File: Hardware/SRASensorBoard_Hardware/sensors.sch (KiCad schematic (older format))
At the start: 10 parts

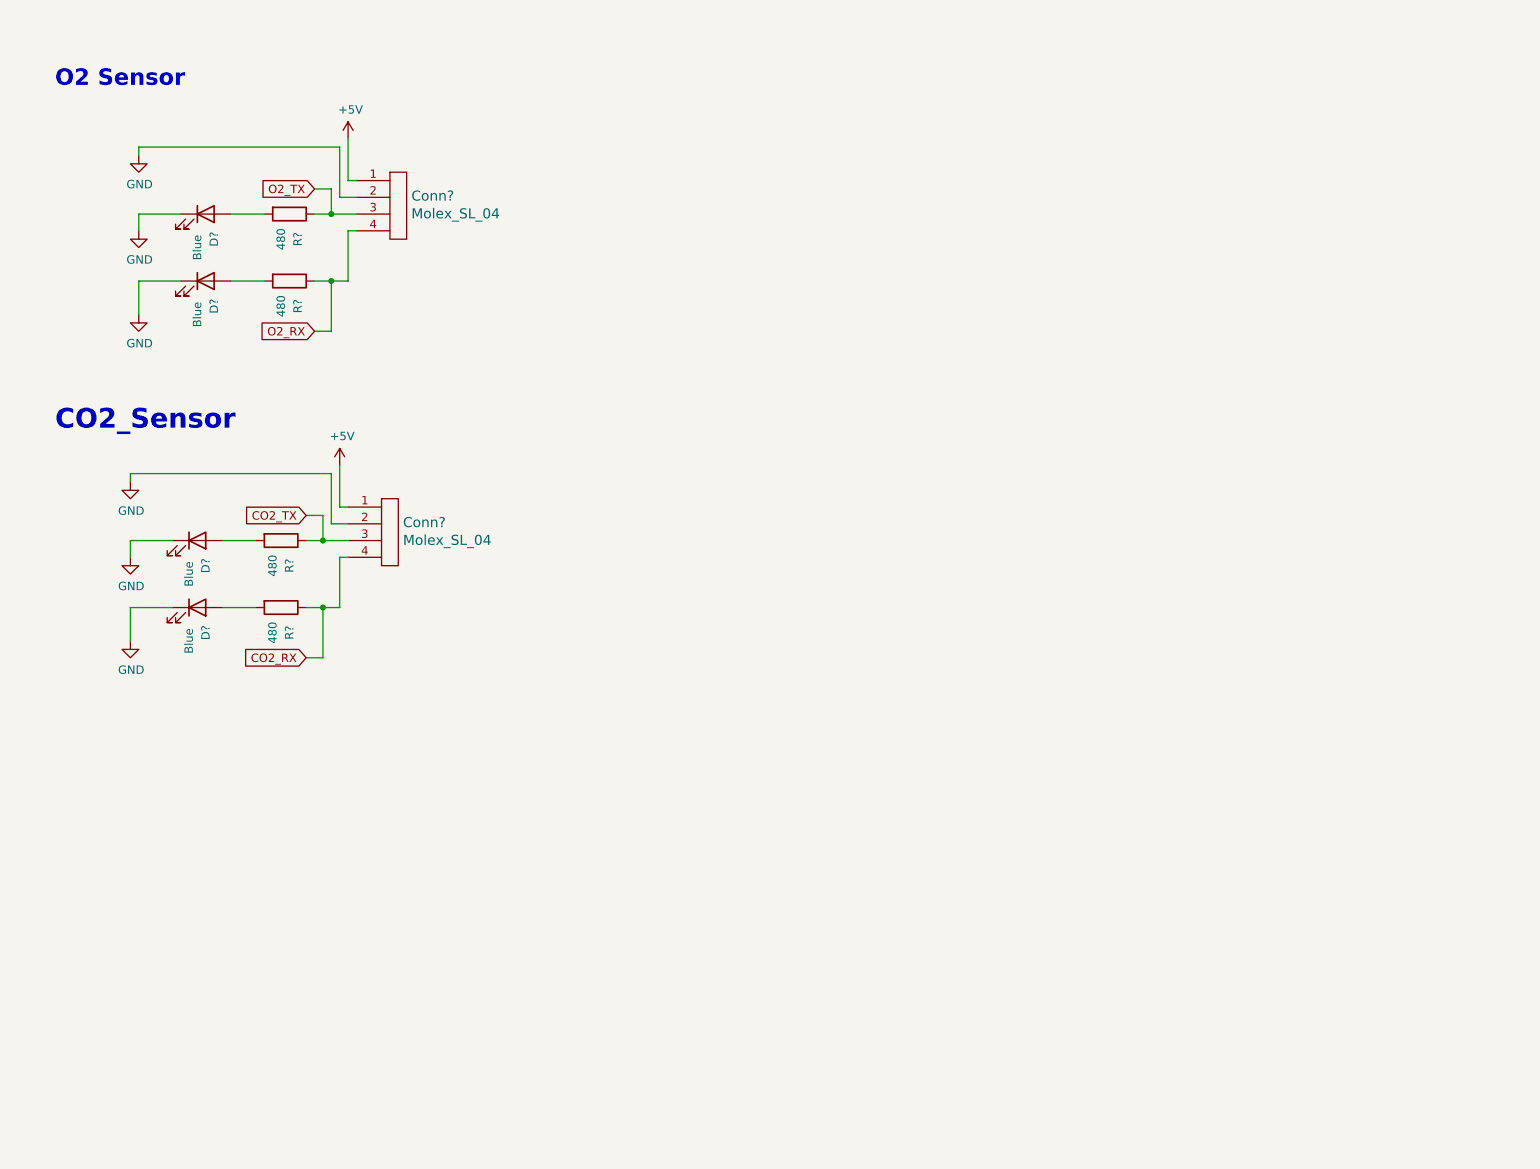
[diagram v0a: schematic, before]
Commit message: Methane Sensor & Tiva Pins added
Added USB A connector and USB to UART converter for CH4 sensor
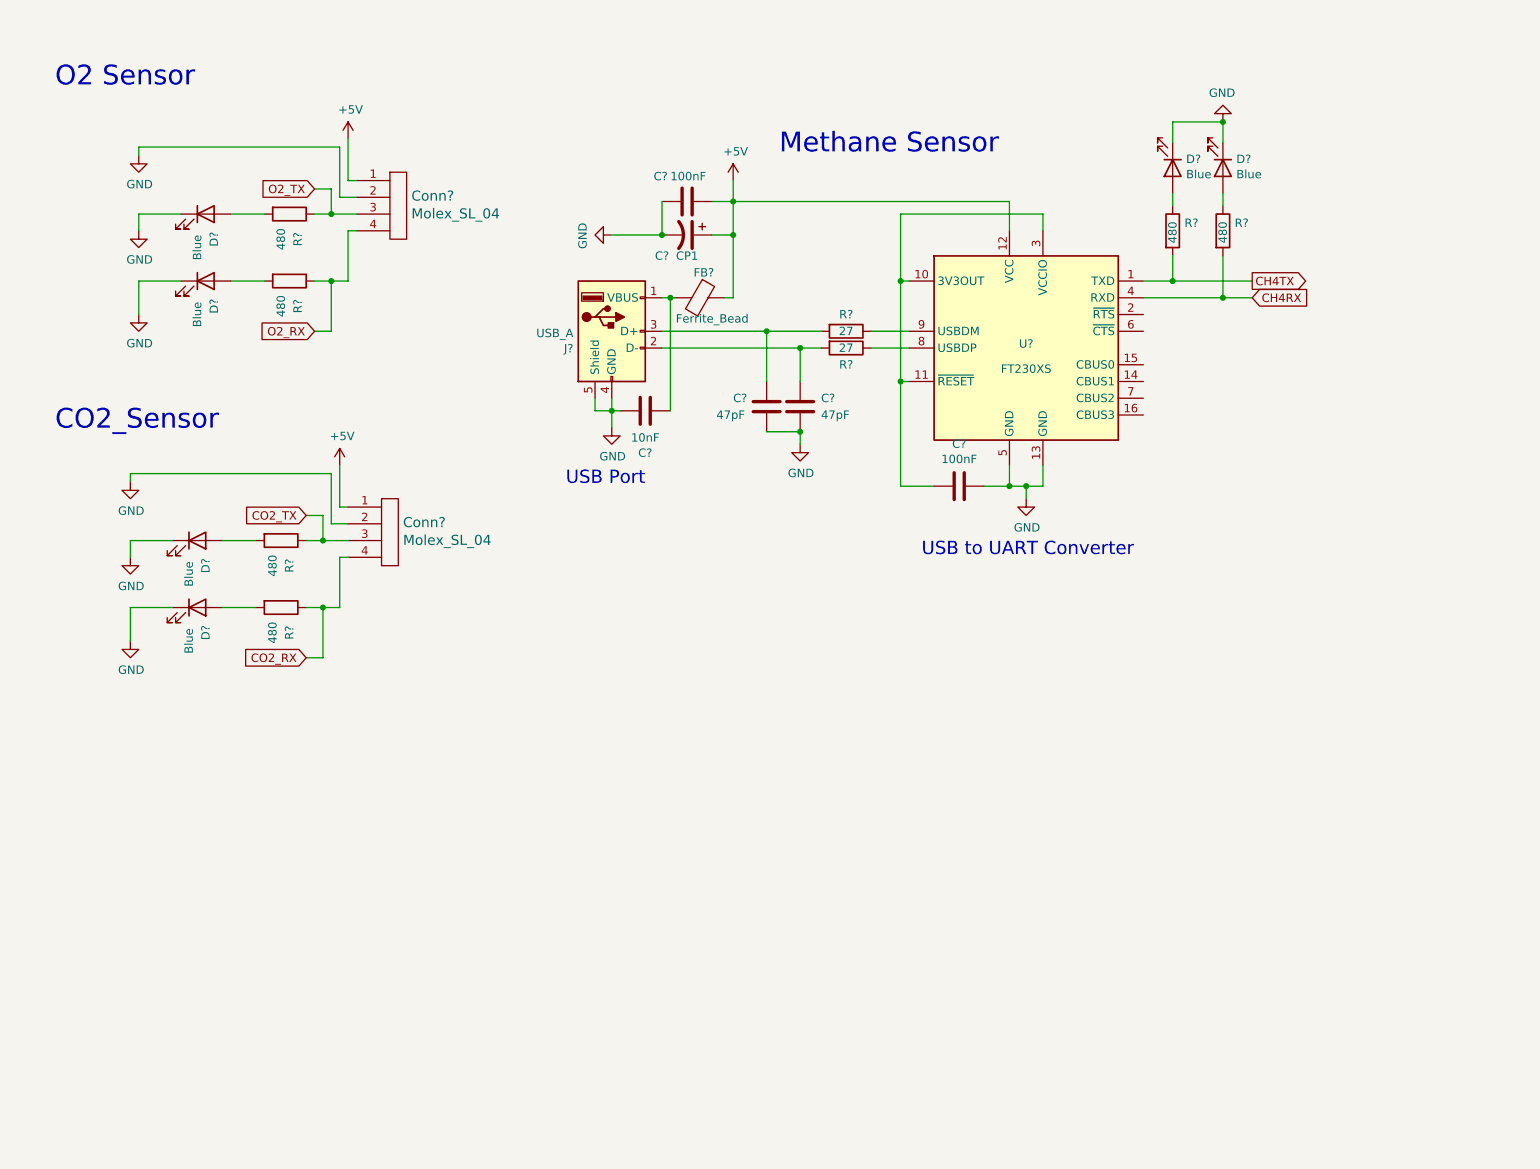
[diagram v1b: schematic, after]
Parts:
- added C?: 10nF, symbol Device:C
- added C? (x2): 47pF, symbol Device:C
- added C? (x2): 100nF, symbol Device:C
- added C?: CP1, symbol Device:CP1
- added D? (x2): Blue, symbol Device:LED
- added FB?: Ferrite_Bead, symbol Device:Ferrite_Bead
- added J?: USB_A, symbol Connector:USB_A
- added R? (x2): 27, symbol Device:R
- added R? (x2): 480, symbol Device:R
- added U?: FT230XS, Package_SO:SSOP-16_3.9x4.9mm_P0.635mm, symbol Interface_USB:FT230XS
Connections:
- net +5V: now also C?.1, C?.1, FB?.1, U?.12 (VCC)
- net GND: now also C?.1, C?.2, C?.2, C?.2, C?.2, C?.2, D?.1 (K), D?.1 (K), J?.4 (GND), J?.5 (Shield), U?.13 (GND), U?.5 (GND)
- new net: C?.1, U?.10 (3V3OUT), U?.11 (~RESET), U?.3 (VCCIO)
- new net: R?.1, U?.8 (USBDP)
- new net: R?.1, U?.9 (USBDM)
- new net: C?.2, FB?.2, J?.1 (VBUS)
- new net: C?.1, J?.2 (D-), R?.2
- new net: C?.1, J?.3 (D+), R?.2
- new net: D?.2 (A), R?.1 (x2)
- new net CH4RX: R?.2, U?.4 (RXD)
- new net CH4TX: R?.2, U?.1 (TXD)
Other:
- note added: "Methane Sensor"
- note added: "USB Port"
- note added: "USB to UART Converter"

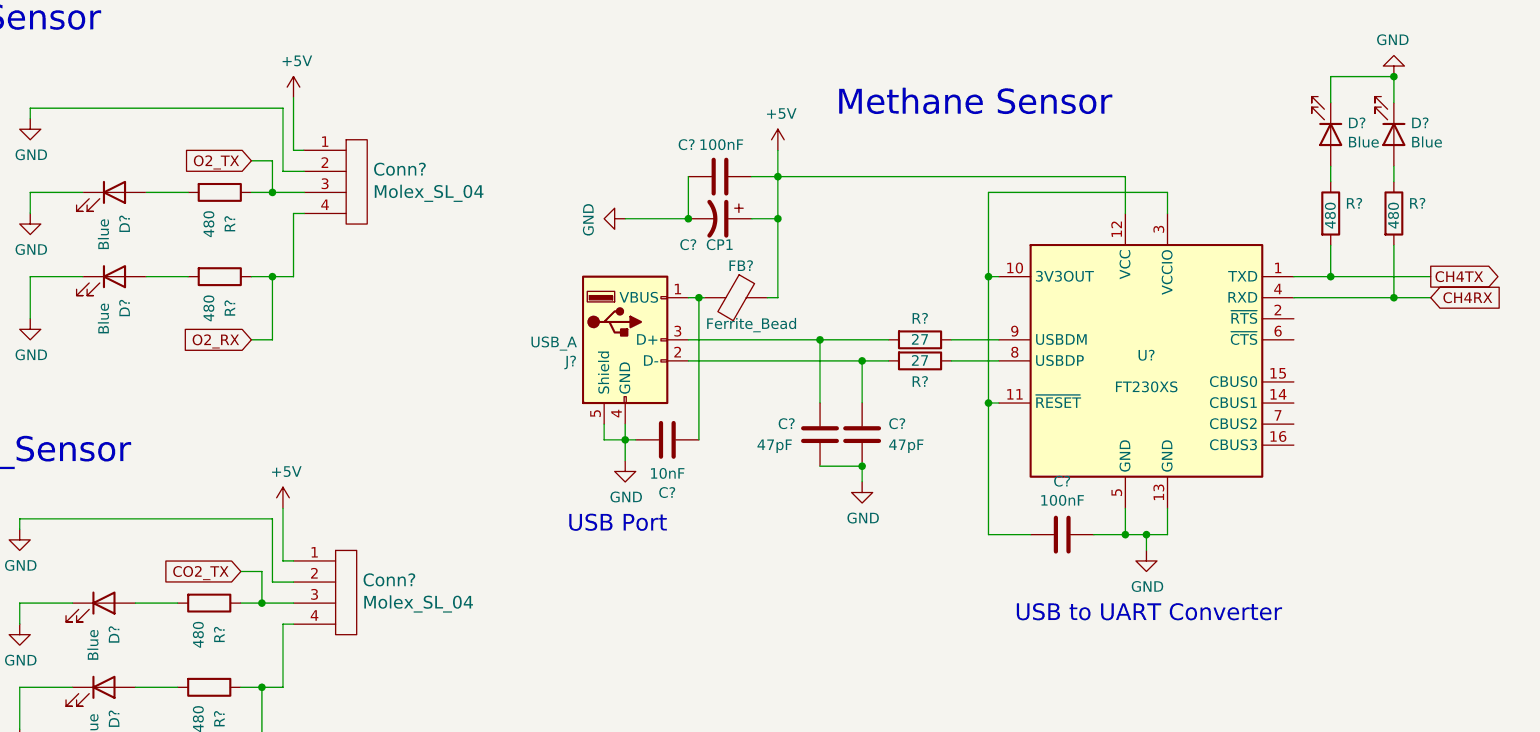
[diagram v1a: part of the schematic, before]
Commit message: Renamed CH4 RX/TX to match with others, swapped tx&rx tiva pins (might be wrong)
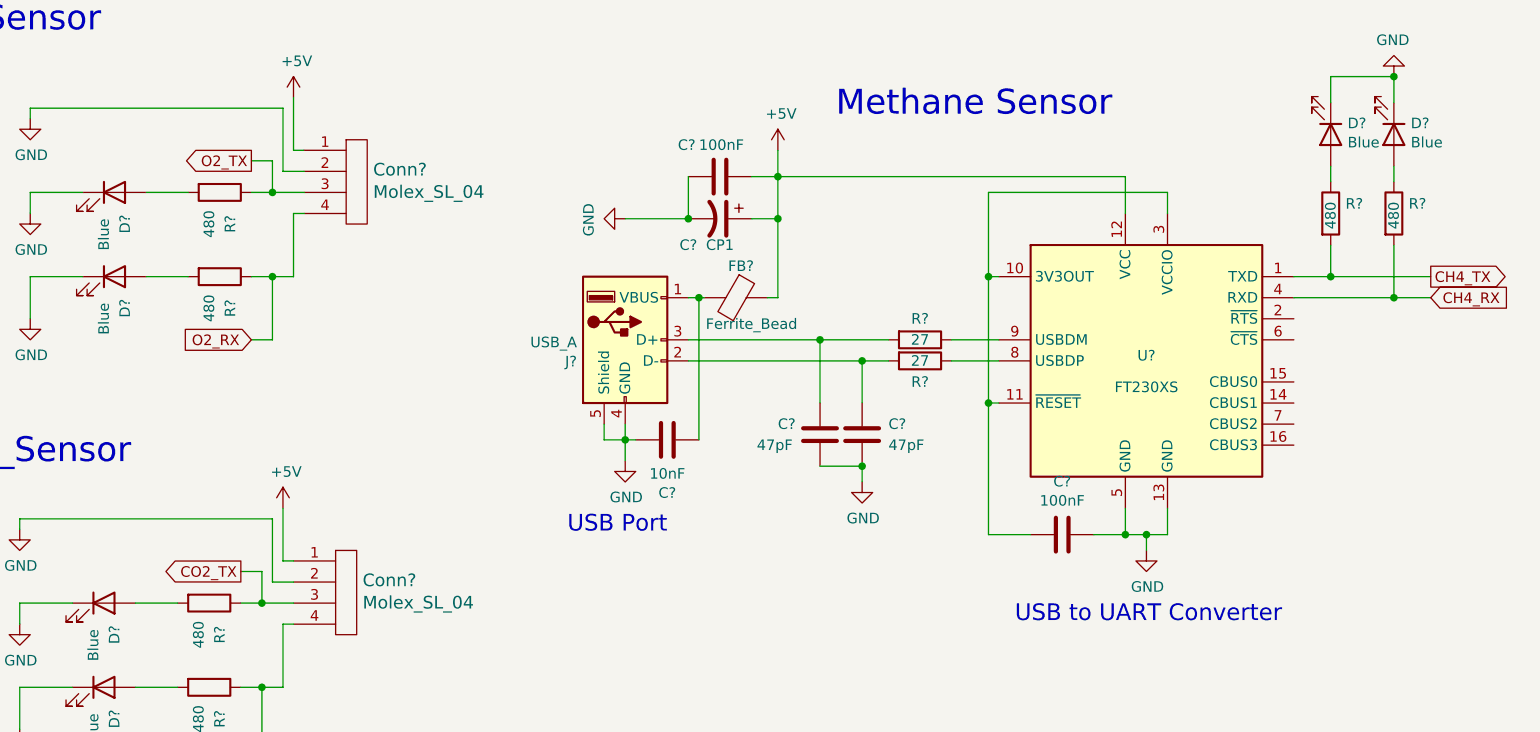
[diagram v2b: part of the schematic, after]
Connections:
- net CH4RX renamed CH4_RX
- net CH4TX renamed CH4_TX
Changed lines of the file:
@@
 Wire Wire Line
 	2450 1750 2600 1750
-Text GLabel 2350 1600 0    50   Input ~ 0
+Text GLabel 2350 1600 0    50   Output ~ 0
 O2_TX
 Wire Wire Line
@@
 Wire Wire Line
 	2400 3700 2550 3700
-Text GLabel 2300 3550 0    50   Input ~ 0
+Text GLabel 2300 3550 0    50   Output ~ 0
 CO2_TX
 Wire Wire Line
@@
 	7300 2250 7775 2250
 Text GLabel 7950 2250 2    50   Input ~ 0
-CH4RX
+CH4_RX
 Text GLabel 7950 2150 2    50   Output ~ 0
-CH4TX
+CH4_TX
 $Comp
 L Device:R R?

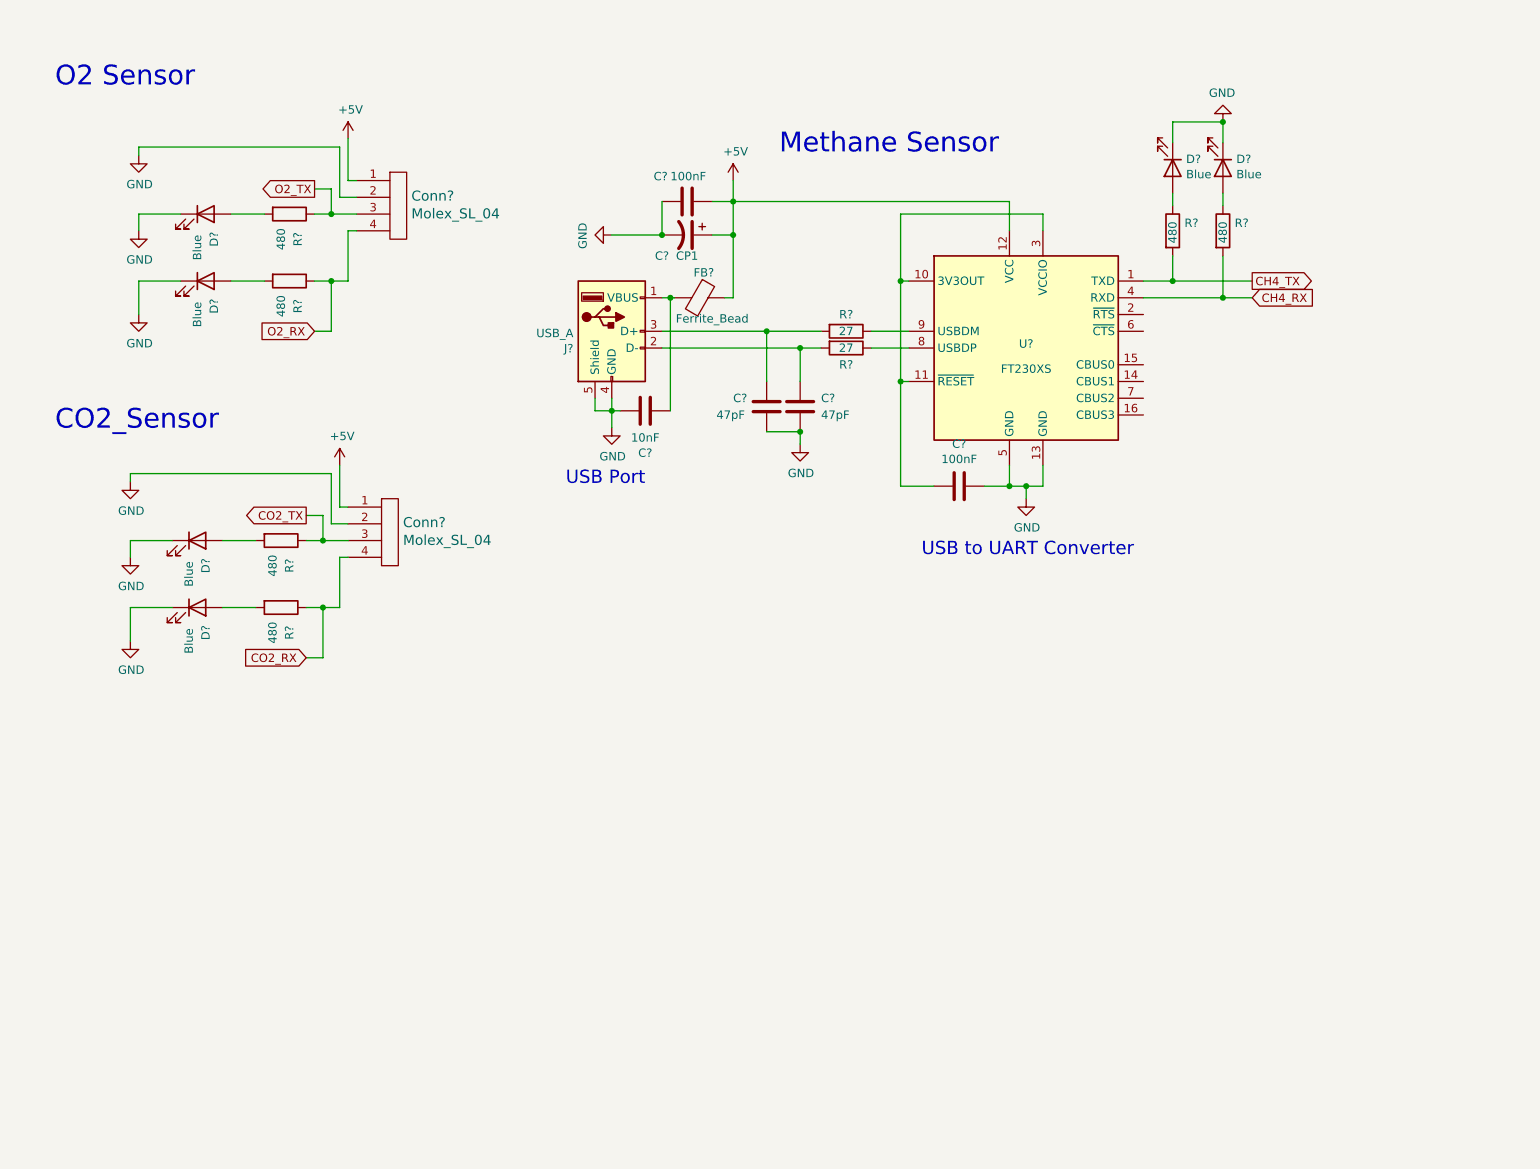
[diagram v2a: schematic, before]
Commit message: Added NH3 sensor and MOSFETS, fixed tiva pins
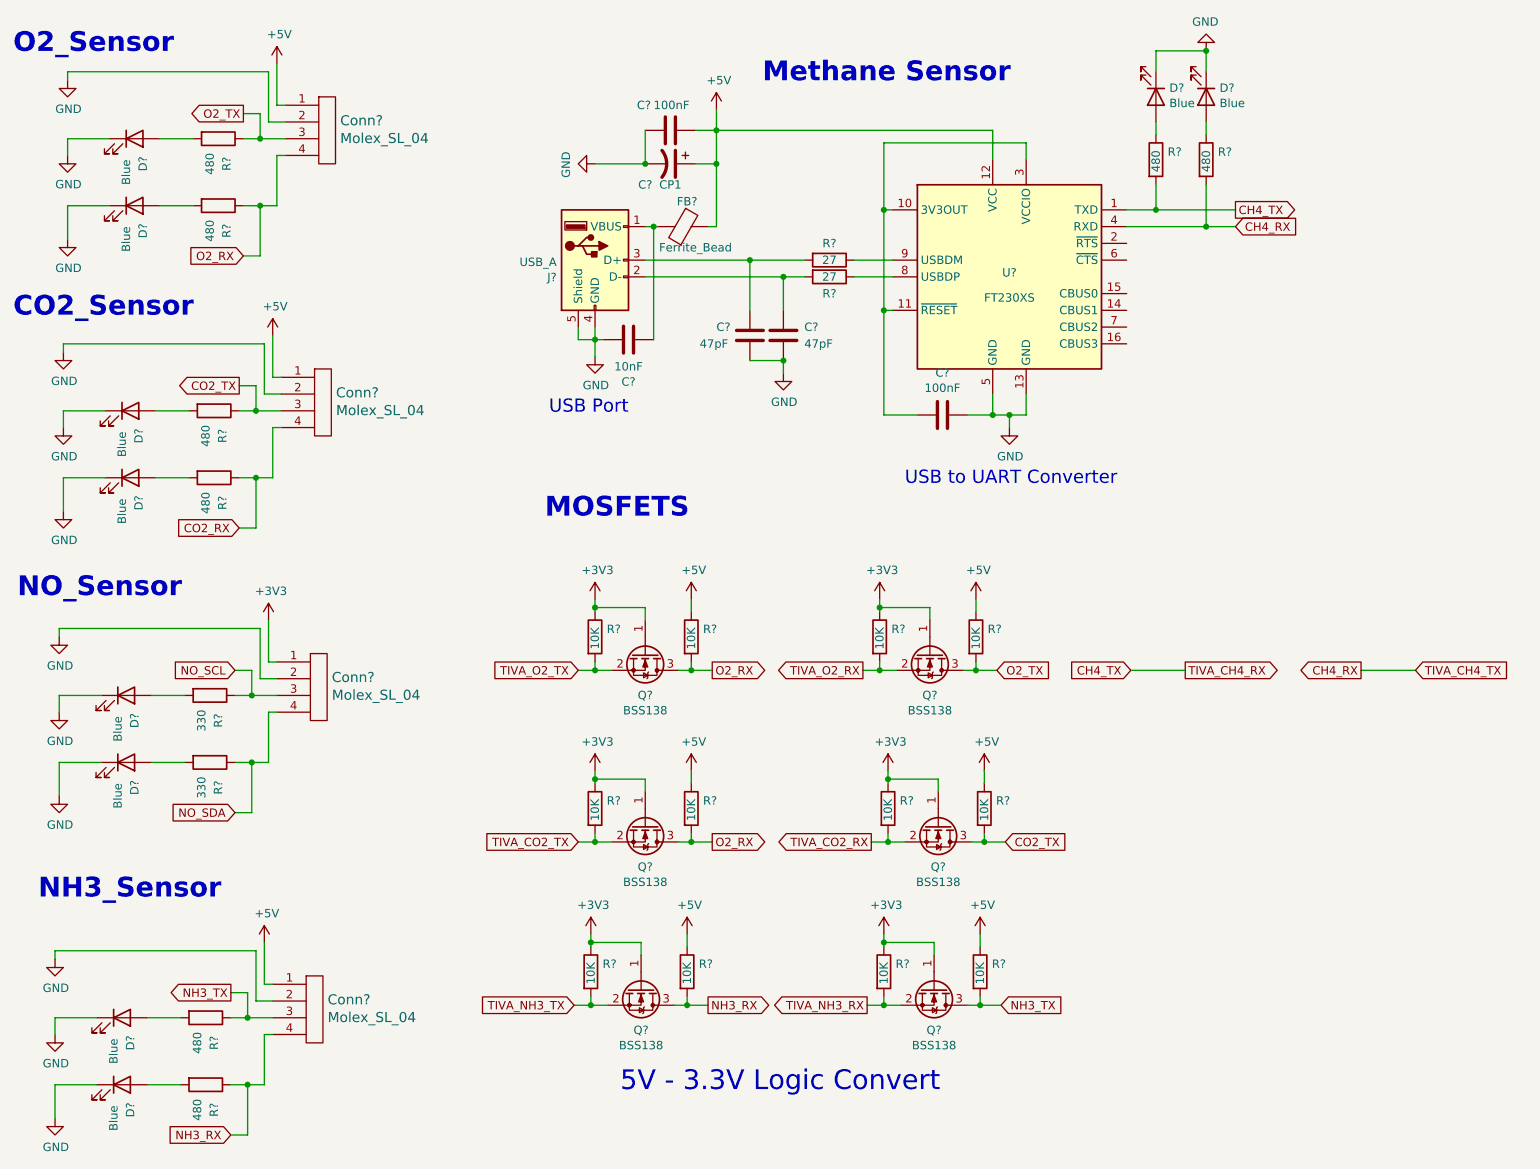
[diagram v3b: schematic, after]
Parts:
- added Conn? (x2): Molex_SL_04, symbol MRDT_Connectors:Molex_SL_04
- added D? (x4): Blue, symbol Device:LED
- added Q? (x6): BSS138, Package_TO_SOT_SMD:SOT-23, symbol Transistor_FET:BSS138
- added R? (x2): 330, symbol Device:R
- added R? (x12): 10K, symbol Device:R
- added R? (x2): 480, symbol Device:R
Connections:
- net +5V: now also Conn?.1, R?.1, R?.1, R?.1, R?.1, R?.1, R?.1
- net CO2_TX: now also Q?.3 (D), R?.2
- net GND: now also Conn?.2, Conn?.2, D?.1 (K), D?.1 (K), D?.1 (K), D?.1 (K)
- net O2_RX: now also Q?.3 (D), Q?.3 (D), R?.2, R?.2
- net O2_TX: now also Q?.3 (D), R?.2
- new net: D?.2 (A), R?.2 (x4)
- new net +3V3: Conn?.1, Q?.1 (G), Q?.1 (G), Q?.1 (G), Q?.1 (G), Q?.1 (G), Q?.1 (G), R?.1, R?.1, R?.1, R?.1, R?.1, R?.1
- new net NH3_RX: Conn?.4, Q?.3 (D), R?.1, R?.2
- new net NH3_TX: Conn?.3, Q?.3 (D), R?.1, R?.2
- new net NO_SCL: Conn?.3, R?.1
- new net NO_SDA: Conn?.4, R?.1
- new net TIVA_CO2_RX: Q?.2 (S), R?.2
- new net TIVA_CO2_TX: Q?.2 (S), R?.2
- new net TIVA_NH3_RX: Q?.2 (S), R?.2
- new net TIVA_NH3_TX: Q?.2 (S), R?.2
- new net TIVA_O2_RX: Q?.2 (S), R?.2
- new net TIVA_O2_TX: Q?.2 (S), R?.2
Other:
- note added: "5V - 3.3V Logic Convert"
- note added: "MOSFETS"
- note added: "NH3_Sensor"
- note added: "NO_Sensor"
- note added: "O2_Sensor"
- note removed: "O2 Sensor"
- moved on the sheet: C?, Conn?, D?, FB?, J?, R?, U?

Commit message: schematic review meeting
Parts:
- J1: renamed from J?; symbol Connector:USB_A -> SRA_Sensor_Board-rescue:USB_A-Connector
- R8, R9: renamed from R?; value 330 -> 43
- gave numbers to parts that had none: 50
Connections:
- no-connect marks 0 -> 6
